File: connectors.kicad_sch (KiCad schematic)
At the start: 25 parts, among them J1 Step Bushing, J10 IPT1-110-01-L-D, J11 0430450409, J12 0430450409, J13 0430450409, J14 0430450409, J2 Step Bushing, J3 Step Bushing, J4 Step Bushing, J5 Step Bushing, J6 Step Bushing, J7 Step Bushing, J8 Step Bushing, J9 Step Bushing

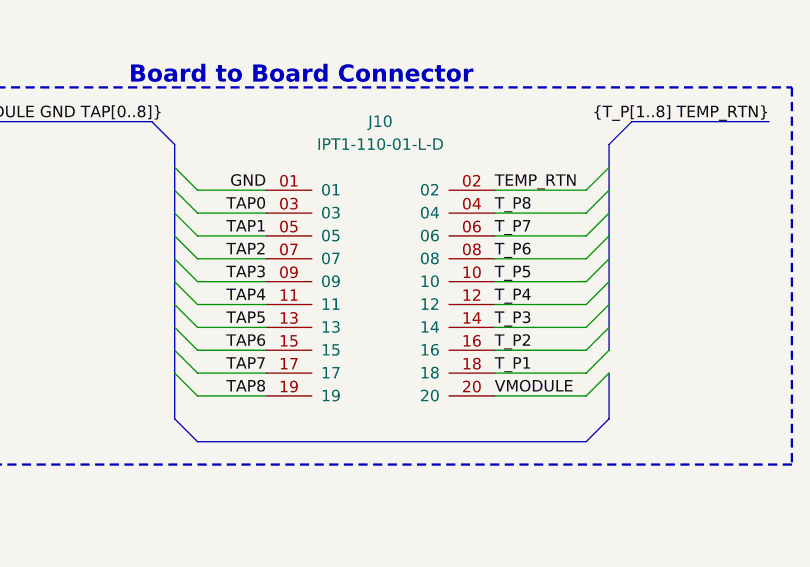
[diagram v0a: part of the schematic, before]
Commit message: PCB[Routing, Layout]: Need to finish routing ground for temp, and ensure its fine to combine on bms board or route to correct ground plane. Layout mostly done need to check interface in module cad.
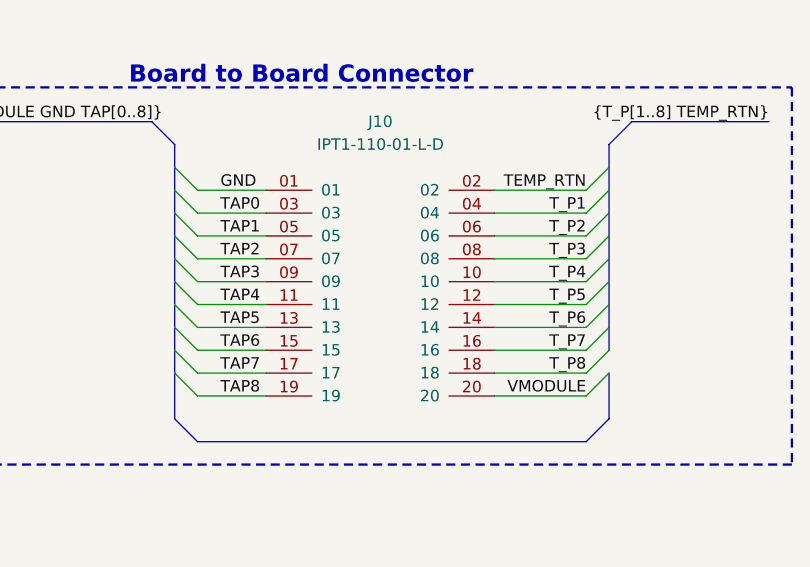
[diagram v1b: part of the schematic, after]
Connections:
- net T_P1: now also J10.04; no longer J10.18
- net T_P2: now also J10.06; no longer J10.16
- net T_P3: now also J10.08; no longer J10.14
- net T_P4: now also J10.10; no longer J10.12
- net T_P5: now also J10.12; no longer J10.10
- net T_P6: now also J10.14; no longer J10.08
- net T_P7: now also J10.16; no longer J10.06
- net T_P8: now also J10.18; no longer J10.04

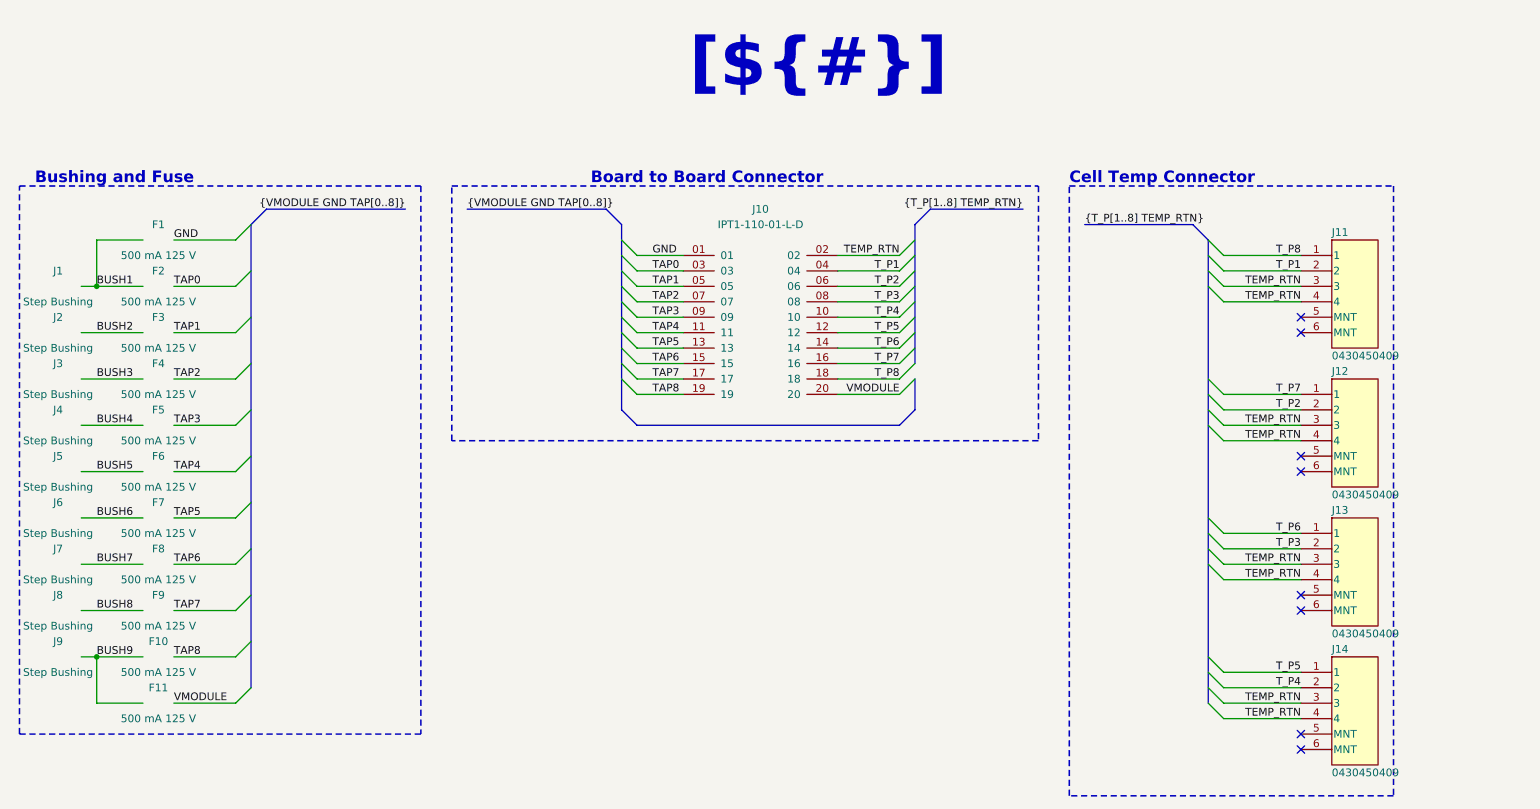
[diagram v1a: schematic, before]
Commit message: PCB[Mounting]: Added standoffs going to test clearnaces. SCH[Mechanical]: Added standoffs, 14mm metal smt, small naming changes to match bms_slave sch.
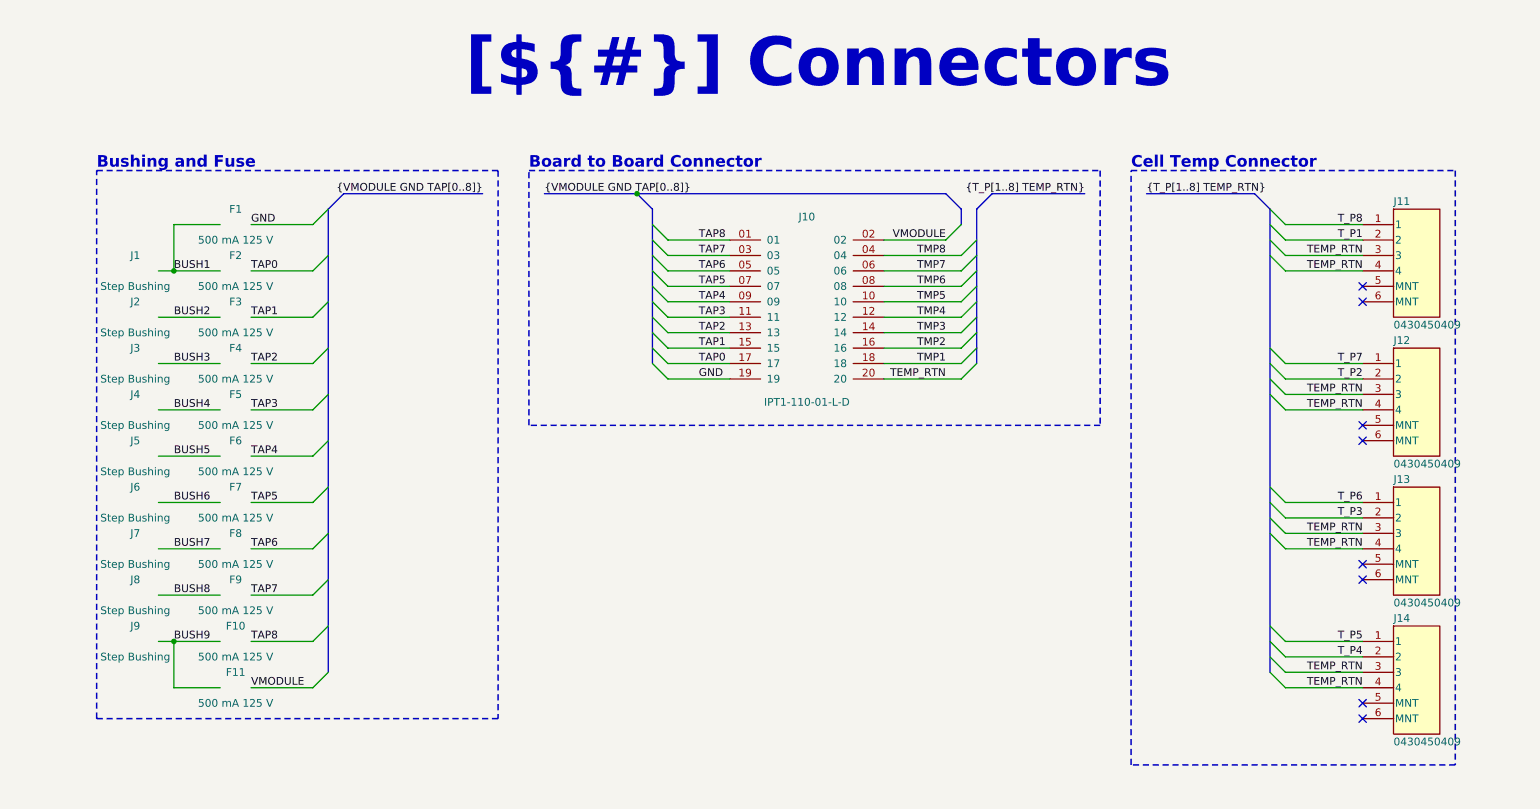
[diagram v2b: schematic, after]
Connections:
- net GND: now also J10.19; no longer J10.01
- net TAP0: now also J10.17; no longer J10.03
- net TAP1: now also J10.15; no longer J10.05
- net TAP2: now also J10.13; no longer J10.07
- net TAP3: now also J10.11; no longer J10.09
- net TAP4: now also J10.09; no longer J10.11
- net TAP5: now also J10.07; no longer J10.13
- net TAP6: now also J10.05; no longer J10.15
- net TAP7: now also J10.03; no longer J10.17
- net TAP8: now also J10.01; no longer J10.19
- net TEMP_RTN: now also J10.20; no longer J10.02
- net T_P1: no longer J10.04
- net T_P2: no longer J10.06
- net T_P3: no longer J10.08
- net T_P4: no longer J10.10
- net T_P5: no longer J10.12
- net T_P6: no longer J10.14
- net T_P7: no longer J10.16
- net T_P8: no longer J10.18
- net VMODULE: now also J10.02; no longer J10.20
- new net TMP1: J10.18
- new net TMP2: J10.16
- new net TMP3: J10.14
- new net TMP4: J10.12
- new net TMP5: J10.10
- new net TMP6: J10.08
- new net TMP7: J10.06
- new net TMP8: J10.04
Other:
- title: (none) -> Connectors
- moved on the sheet: J11, J12, J13, J14

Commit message: PCB[Routing, Mechanical, Silk]: Inital routing, Finalized mounting points and board to board connector reltive posision, and inital silkscreen. SCH[Labels]: Updated labels to match BMS_Slave board.
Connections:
- net T_P1 is gone; now on net TMP1: J11.2
- net T_P2 is gone; now on net TMP2: J12.2
- net T_P3 is gone; now on net TMP3: J13.2
- net T_P4 is gone; now on net TMP4: J14.2
- net T_P5 is gone; now on net TMP5: J14.1
- net T_P6 is gone; now on net TMP6: J13.1
- net T_P7 is gone; now on net TMP7: J12.1
- net T_P8 is gone; now on net TMP8: J11.1
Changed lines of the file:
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@@
 		)
 	)
-	(label "T_P2"
+	(label "TMP2"
 		(at 243.84 76.2 180)
 		(effects
@@
 		)
 	)
-	(label "T_P5"
+	(label "TMP5"
 		(at 243.84 119.38 180)
 		(effects
@@
 		)
 	)
-	(label "{T_P[1..8] TEMP_RTN}"
+	(label "{TMP[1..8] TEMP_RTN}"
 		(at 208.28 45.72 0)
 		(fields_autoplaced yes)
@@
 		)
 	)
-	(label "T_P1"
+	(label "TMP1"
 		(at 243.84 53.34 180)
 		(effects
@@
 		)
 	)
-	(label "T_P6"
+	(label "TMP6"
 		(at 243.84 96.52 180)
 		(effects
@@
 		)
 	)
-	(label "T_P3"
+	(label "TMP3"
 		(at 243.84 99.06 180)
 		(effects
@@
 		)
 	)
-	(label "{T_P[1..8] TEMP_RTN}"
+	(label "{TMP[1..8] TEMP_RTN}"
 		(at 198.12 45.72 180)
 		(fields_autoplaced yes)
@@
 		)
 	)
-	(label "T_P4"
+	(label "TMP4"
 		(at 243.84 121.92 180)
 		(effects
@@
 		)
 	)
-	(label "T_P7"
+	(label "TMP7"
 		(at 243.84 73.66 180)
 		(effects
@@
 		)
 	)
-	(label "T_P8"
+	(label "TMP8"
 		(at 243.84 50.8 180)
 		(effects

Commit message: PCB[Connector, Clearnces]: Testing clearances.
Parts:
- removed J1, J2, J3, J4, J5, J6, J7, J8, J9: Step Bushing, remote_n_a:steped_bushing, symbol remote_n_a:Steped_Bushing
- removed J11, J12, J13, J14: 0430450409, remote_0430450409:CONN_SD-43045-004_04_MOL, symbol remote_0430450409:430450409
- added J1, J2, J3, J4: 0436500412, remote_0436500412:CONN_SD-43650-005_04_MOL, symbol remote_0436500412:0436500412
- added MP10, MP11, MP12, MP13, MP5, MP6, MP7, MP8, MP9: Enepaq M5 Clamp, remote_enepaq_m5_clamp:Enepaq_M5_Clamp, symbol remote_enepaq_m5_clamp:Enepaq_M5_Clamp
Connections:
- net BUSH1: now also MP5.1
- net BUSH2: now also MP6.1
- net BUSH3: now also MP7.1
- net BUSH4: now also MP8.1
- net BUSH5: now also MP9.1
- net BUSH6: now also MP10.1
- net BUSH7: now also MP11.1
- net BUSH8: now also MP12.1
- net BUSH9: now also MP13.1
- net TEMP_RTN: now also J1.3, J1.4, J2.3, J2.4, J3.3, J3.4, J4.3, J4.4
- net TMP1: now also J1.2
- net TMP2: now also J2.2
- net TMP3: now also J3.2
- net TMP4: now also J4.2
- net TMP5: now also J4.1
- net TMP6: now also J3.1
- net TMP7: now also J2.1
- net TMP8: now also J1.1

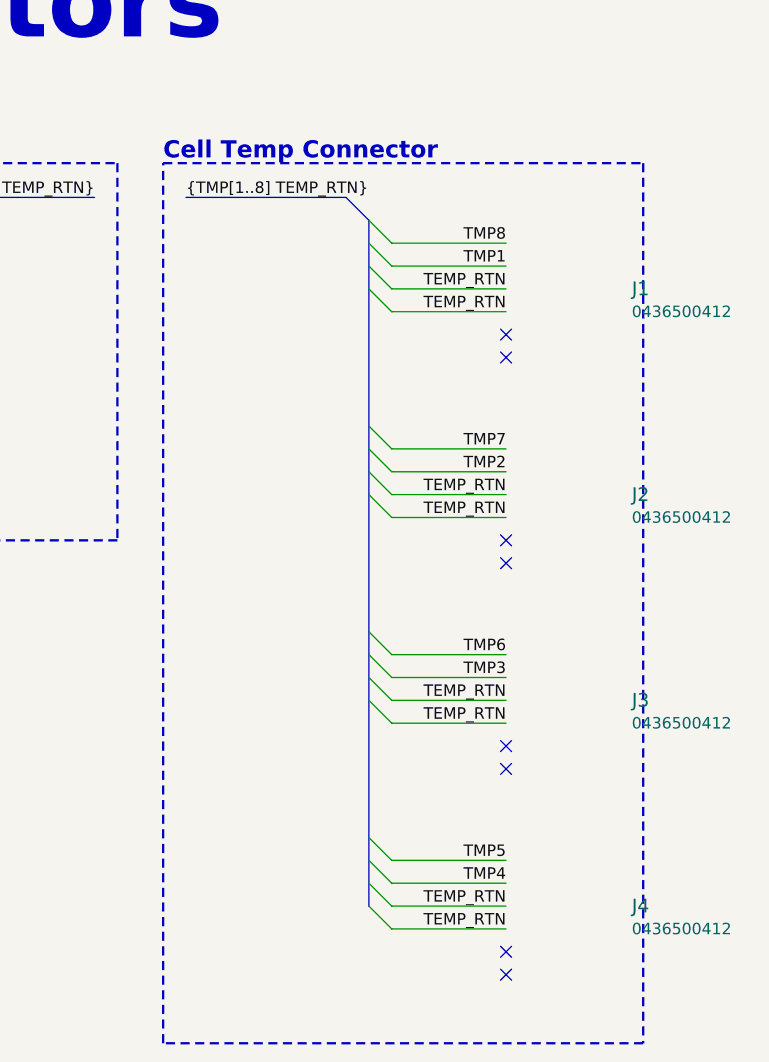
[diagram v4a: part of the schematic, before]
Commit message: PCB[Routing, Mount]: Did intial routing and clearnce, Changed connector from Microfit 3.0 to JST XH STM 4 Position. More room and mating end fit fully on board surface. Need to update standoffs, and samtech board to board connctor.
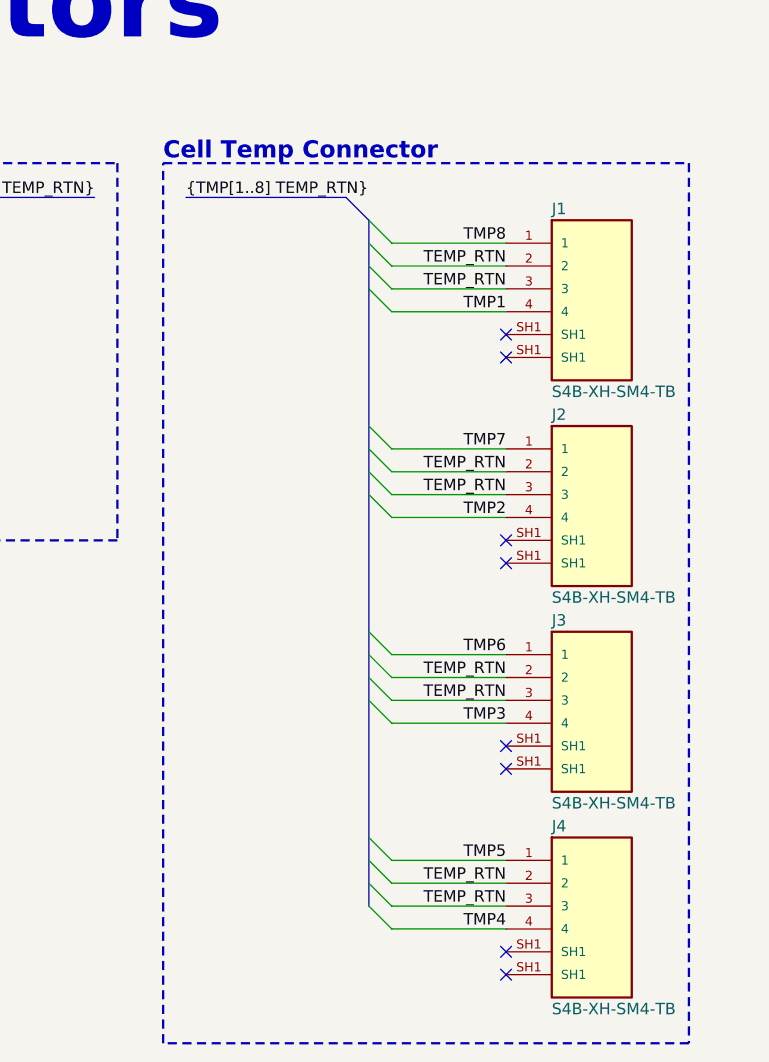
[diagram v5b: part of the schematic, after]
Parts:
- removed J1, J2, J3, J4: 0436500412, remote_0436500412:CONN_SD-43650-005_04_MOL, symbol remote_0436500412:0436500412
- added J1, J2, J3, J4: S4B-XH-SM4-TB, remote_s4b-xh-sm4-tb:JST_S4B-XH-SM4-TB, symbol remote_s4b-xh-sm4-tb:S4B-XH-SM4-TB
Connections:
- net TEMP_RTN: now also J1.2, J1.3, J2.2, J2.3, J3.2, J3.3, J4.2, J4.3
- net TMP1: now also J1.4
- net TMP2: now also J2.4
- net TMP3: now also J3.4
- net TMP4: now also J4.4
- net TMP5: now also J4.1
- net TMP6: now also J3.1
- net TMP7: now also J2.1
- net TMP8: now also J1.1
